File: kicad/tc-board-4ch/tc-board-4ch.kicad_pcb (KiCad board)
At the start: 2 copper layers, 96 x 66 mm, 86 parts, among them J1 HOST, J101 DG127-5.08-02P, J2 BUTTON, J201 DG127-5.08-02P, J301 DG127-5.08-02P, J401 DG127-5.08-02P, U1 SN74AHC125DR, U101 MAX31855KASA+, U102 ISO7731DWR, U103 NCP1117ST33T3G, U201 MAX31855KASA+, U202 ISO7731DWR, U203 NCP1117ST33T3G, U301 MAX31855KASA+, U302 ISO7731DWR, U303 NCP1117ST33T3G, U401 MAX31855KASA+, U402 ISO7731DWR, U403 NCP1117ST33T3G

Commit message: Layout session 2: ground zones in, fills verified, DRC clean on copper
- Five multi-layer zones: host GND strip and four GND_ISO islands, 0.3
  clearance, thermal reliefs; 2 mm bare gap between islands, slots
  between host and islands
- Fills checked by refilled scratch copy and SVG export; 0 clearance,
  isolation or edge violations
- Five starved-thermal errors on isolator GND1 pins and C105 noted, to
  clear with the GND tie tracks during routing
- Layout session 1 rolled into docs/archive; routing channel 1 is next

Co-Authored-By: Claude Fable 5.1 <noreply@anthropic.com>
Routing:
- added copper zone on B.Cu, net /CH1/GND_ISO
- added copper zone on F.Cu, net /CH1/GND_ISO
- added copper zone on B.Cu, net /CH2/GND_ISO
- added copper zone on F.Cu, net /CH2/GND_ISO
- added copper zone on B.Cu, net /CH3/GND_ISO
- added copper zone on F.Cu, net /CH3/GND_ISO
- added copper zone on B.Cu, net /CH4/GND_ISO
- added copper zone on F.Cu, net /CH4/GND_ISO
- added copper zone on B.Cu, net GND
- added copper zone on F.Cu, net GND
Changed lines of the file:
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@@
 		(layer "Edge.Cuts")
+	)
+	(zone
+		(net "/CH4/GND_ISO")
+		(layers "F.Cu" "B.Cu")
+		(hatch edge 0.5)
+		(priority 4)
+		(connect_pads
+			(clearance 0.3)
+		)
+		(min_thickness 0.25)
+		(fill yes
+			(thermal_gap 0.5)
+			(thermal_bridge_width 0.5)
+			(island_removal_mode 0)
+		)
+		(polygon
+			(pts
+				(xy 121 68) (xy 141 68) (xy 141 115.5) (xy 121 115.5)
+			)
+		)
+	)
+	(zone
+		(net "/CH2/GND_ISO")
+		(layers "F.Cu" "B.Cu")
+		(hatch edge 0.5)
+		(priority 2)
+		(connect_pads
+			(clearance 0.3)
+		)
+		(min_thickness 0.25)
+		(fill yes
+			(thermal_gap 0.5)
+			(thermal_bridge_width 0.5)
+			(island_removal_mode 0)
+		)
+		(polygon
+			(pts
+				(xy 77 68) (xy 97 68) (xy 97 115.5) (xy 77 115.5)
+			)
+		)
+	)
+	(zone
+		(net "/CH1/GND_ISO")
+		(layers "F.Cu" "B.Cu")
+		(hatch edge 0.5)
+		(priority 1)
+		(connect_pads
+			(clearance 0.3)
+		)
+		(min_thickness 0.25)
+		(fill yes
+			(thermal_gap 0.5)
+			(thermal_bridge_width 0.5)
+			(island_removal_mode 0)
+		)
+		(polygon
+			(pts
+				(xy 55 68) (xy 75 68) (xy 75 115.5) (xy 55 115.5)
+			)
+		)
+	)
+	(zone
+		(net "GND")
+		(layers "F.Cu" "B.Cu")
+		(hatch edge 0.5)
+		(connect_pads
+			(clearance 0.3)
+		)
+		(min_thickness 0.25)
+		(fill yes
+			(thermal_gap 0.5)
+			(thermal_bridge_width 0.5)
+			(island_removal_mode 0)
+		)
+		(polygon
+			(pts
+				(xy 50.5 50.5) (xy 145.5 50.5) (xy 145.5 65) (xy 50.5 65)
+			)
+		)
+	)
+	(zone
+		(net "/CH3/GND_ISO")
+		(layers "F.Cu" "B.Cu")
+		(hatch edge 0.5)
+		(priority 3)
+		(connect_pads
+			(clearance 0.3)
+		)
+		(min_thickness 0.25)
+		(fill yes
+			(thermal_gap 0.5)
+			(thermal_bridge_width 0.5)
+			(island_removal_mode 0)
+		)
+		(polygon
+			(pts
+				(xy 99 68) (xy 119 68) (xy 119 115.5) (xy 99 115.5)
+			)
+		)
 	)
 	(embedded_fonts no)

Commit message: Layout session 3: all four islands routed, DRC clean on copper
- Channel 1 drawn pad by pad from Claude's order, each save DRC-checked
  and rendered from a scratch copy; channels 2-4 reused the order after
  pad positions were verified as exact +22 mm copies
- Regulator pin 2 to tab needs a copper link (KiCad lists same-numbered
  pads as unconnected); hopped under the 0.4 mm +5V_ISO run on B.Cu
- T+/T- cross once above each terminal; TVS GND pad forces a detour
- Pre-defined track widths 0.4 / 0.25 added so W and the bulk width
  editor work; unconnected 137 -> 37, all host side

Co-Authored-By: Claude Fable 5.1 <noreply@anthropic.com>
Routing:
- net /CH4/+3V3_ISO: track 0.00 -> 48.3 mm, vias 0 -> 4
- net /CH3/+3V3_ISO: track 0.00 -> 48.3 mm, vias 0 -> 4
- net /CH2/+3V3_ISO: track 0.00 -> 48.3 mm, vias 0 -> 4
- net /CH1/+3V3_ISO: track 0.00 -> 48.3 mm, vias 0 -> 4
- net Net-(D402-A2): track 0.00 -> 18.1 mm
- net Net-(D101-A2): track 0.00 -> 18.0 mm, vias 0 -> 2
- net Net-(D401-A2): track 0.00 -> 17.8 mm, vias 0 -> 2
- net Net-(D301-A2): track 0.00 -> 17.7 mm, vias 0 -> 2
- net Net-(D201-A2): track 0.00 -> 17.7 mm, vias 0 -> 2
- net Net-(D102-A2): track 0.00 -> 17.4 mm
- net Net-(D302-A2): track 0.00 -> 17.4 mm
- net Net-(D202-A2): track 0.00 -> 17.4 mm
- net /CH1/+5V_ISO: track 0.00 -> 16.7 mm
- net /CH3/+5V_ISO: track 0.00 -> 16.6 mm
- net /CH2/+5V_ISO: track 0.00 -> 16.6 mm
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
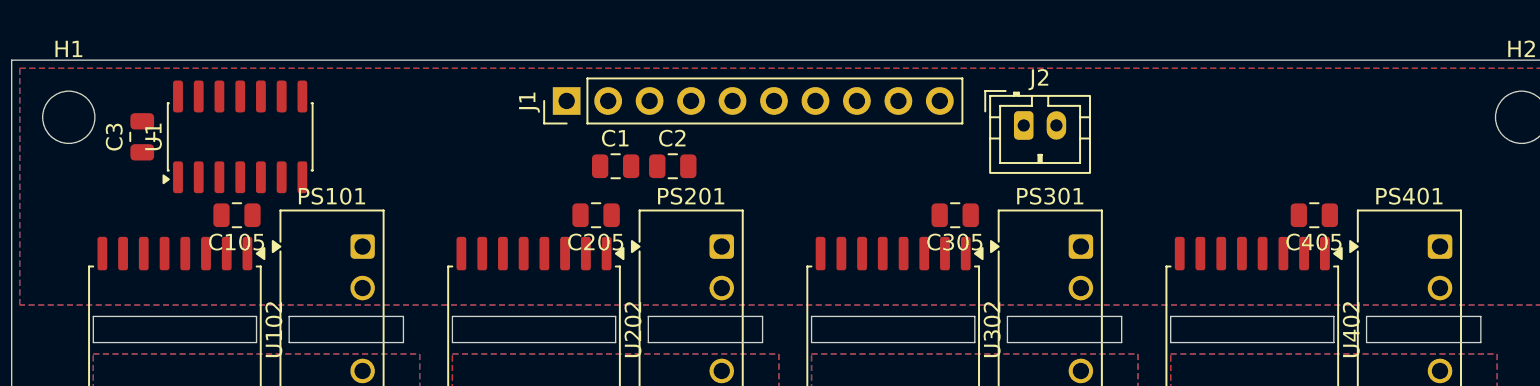
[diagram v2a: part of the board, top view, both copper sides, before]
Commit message: Layout session 5: host routing applied to the real board, verified beyond DRC
- Ran host-routing.py on the real board with the editor closed: 5 part
  moves, 75 tracks, 37 vias; 0 unconnected, 0 copper errors, fills saved
- Verified independently of DRC: netlist parity 276/276, net classes,
  isolation rules proven by planted tracks, zone recess 2.0 mm, measured
  island gaps 2.0/3.0 mm, trace current margin
- kicad-cli 10.0.6 DRC reports nothing for a track inside a foreign pad;
  add geom-audit.py and zone-audit.py to cover that, both validated with
  planted defects and clean on the real board
- Roll layout session 4 into the archive

Co-Authored-By: Claude Fable 5.1 <noreply@anthropic.com>
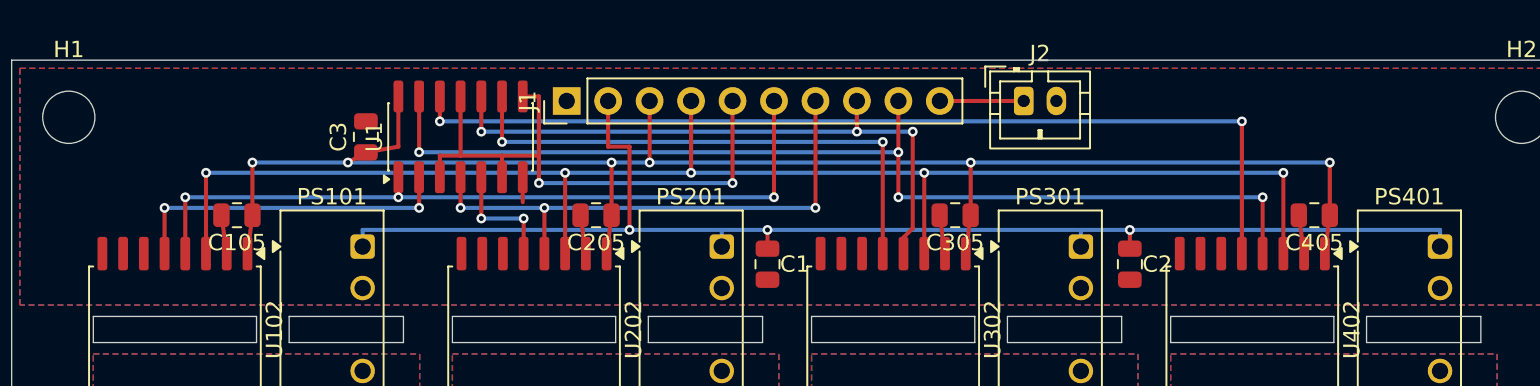
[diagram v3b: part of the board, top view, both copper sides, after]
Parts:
- moved C2 28.6 mm to (118.5, 62.5), turned to -90 degrees
- moved C3 13.7 mm to (71.7, 54.7)
- moved U1 13.5 mm to (77.5, 54.7)
- moved C1 11.1 mm to (96.3, 62.5), turned to -90 degrees
- moved J2 1.50 mm to (112.0, 52.5)
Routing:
- net +3V3: track 0.00 -> 98.5 mm, vias 0 -> 6
- net /SCK: track 0.00 -> 90.2 mm, vias 0 -> 5
- net +5V: track 0.00 -> 81.6 mm, vias 0 -> 3
- net /CS4: track 0.00 -> 64.4 mm, vias 0 -> 4
- net /MISO4: track 0.00 -> 58.8 mm, vias 0 -> 2
- net /CS1: track 0.00 -> 46.6 mm, vias 0 -> 3
- net /CS3: track 0.00 -> 38.2 mm, vias 0 -> 3
- net /MISO: track 0.00 -> 35.5 mm, vias 0 -> 2
- net /CS2: track 0.00 -> 33.0 mm, vias 0 -> 3
- net /MISO3: track 0.00 -> 32.9 mm, vias 0 -> 2
- net /MISO1: track 0.00 -> 20.3 mm, vias 0 -> 2
- net GND: track 0.00 -> 11.0 mm
- net /MISO2: track 0.00 -> 7.27 mm, vias 0 -> 2
- net /BTN: track 0.00 -> 5.14 mm
